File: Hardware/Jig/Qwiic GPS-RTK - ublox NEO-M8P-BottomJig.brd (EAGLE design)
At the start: 40.6 x 33 mm, 103 parts, among them J13 U.FL, J3 PTH, U1 NEO-M8P, U2 3.3V

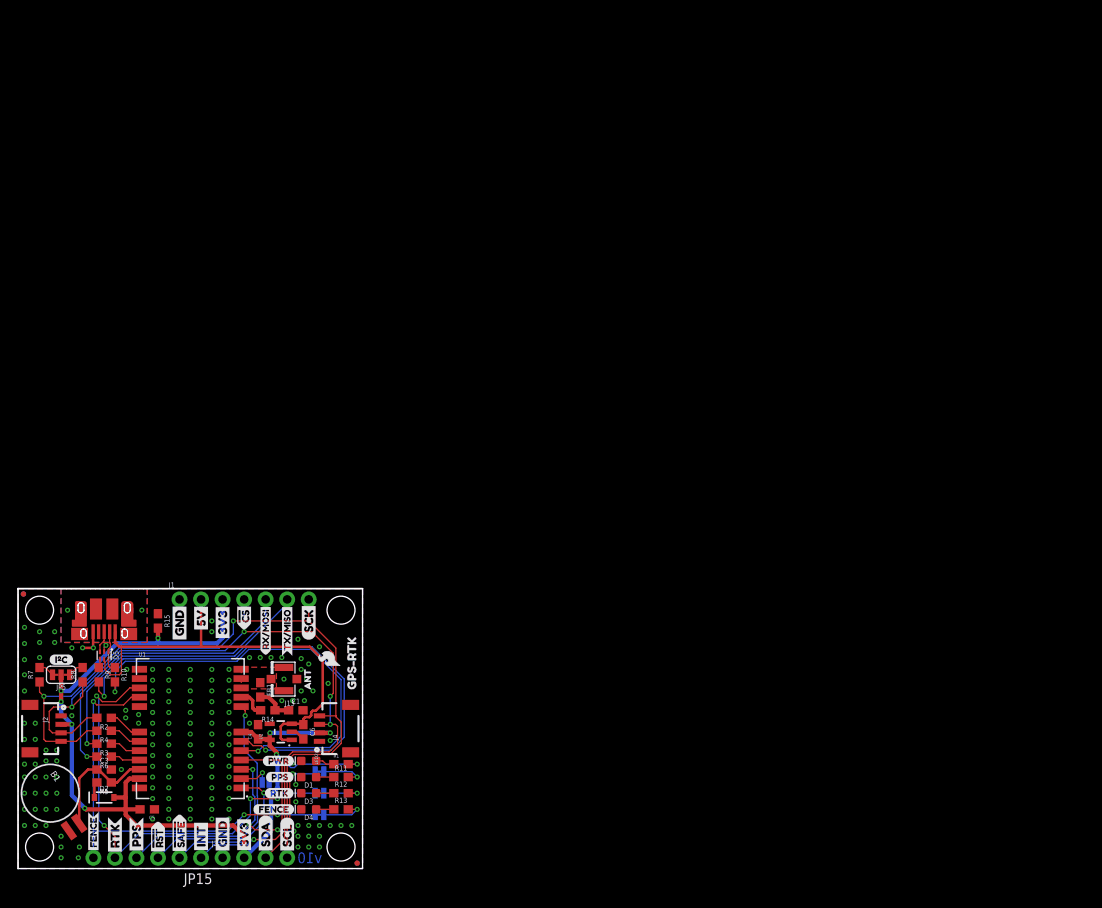
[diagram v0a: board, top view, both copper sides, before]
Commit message: Adding test jig
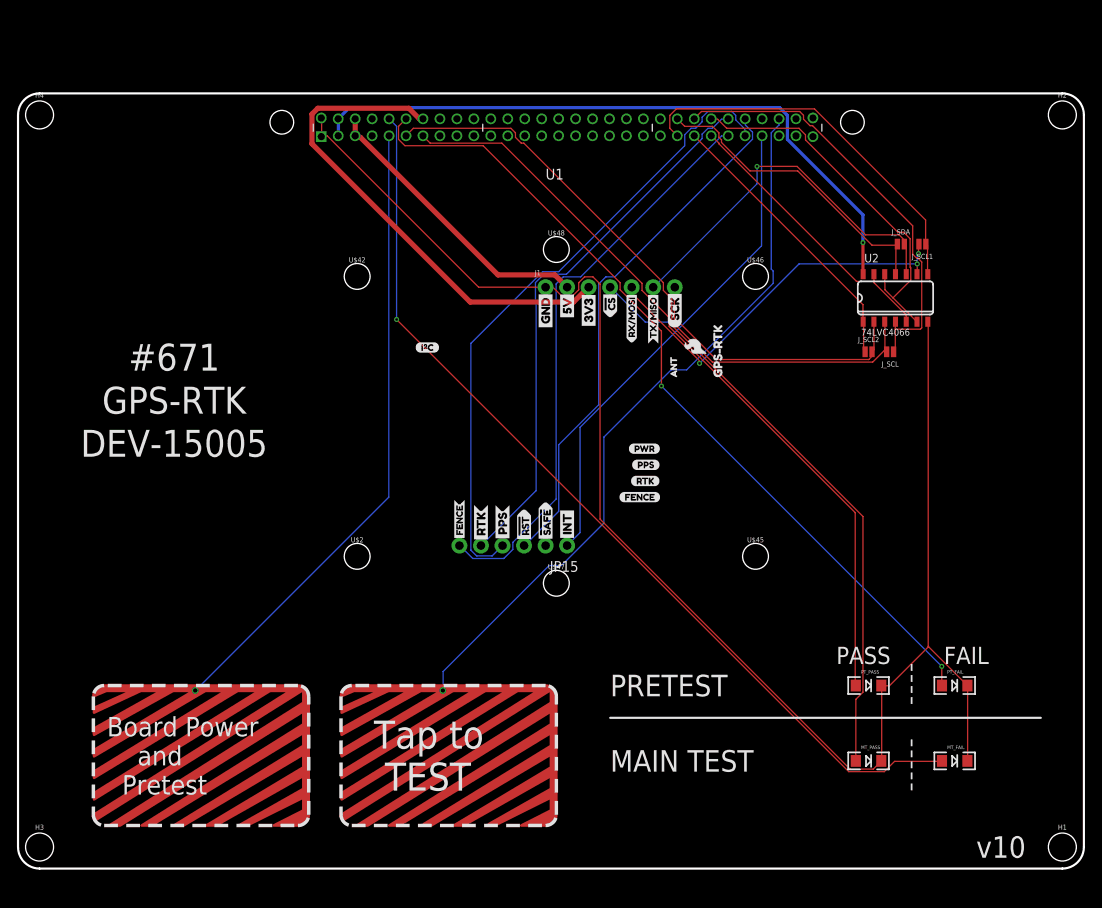
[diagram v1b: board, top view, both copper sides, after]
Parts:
- removed B1: 6.8MM_COIN_CELL, SparkFun-Batteries:BATTCON-6.8MM
- removed C1: 47pF, SparkFun-Capacitors:0603
- removed C3, C4, C6: 1.0uF, SparkFun-Capacitors:0603
- removed C5: 0.1uF, SparkFun-Capacitors:0603
- removed D1: Yellow, SparkFun-LED:LED-0603
- removed D2: 0.5A/40V/420mV, SparkFun-DiscreteSemi:SOD-323
- removed D3: GREEN, SparkFun-LED:LED-0603
- removed D4: BLUE, SparkFun-LED:LED-0603
- removed D5: PRTR5V0U2F, funbit:SOT886
- removed FB1: 30Ω/1.8A, SparkFun-Coils:0603
- removed FRAME1: FRAME-LETTER, SparkFun-Aesthetics:CREATIVE_COMMONS
- removed J13: U.FL, SparkFun-Connectors:U.FL
- removed J2, J4: (no value), SparkFun-Connectors:1X04_1MM_RA
- removed J3: PTH, SparkX:1X04_NO_SILK
- removed J6: (no value), SparkFun-Connectors:USB-MICROB-PTH-MILL
- removed JP1, JP2, JP3: (no value), SparkFun-Jumpers:SMT-JUMPER_2_NC_TRACE_SILK
- removed JP101, JP31, JP41, JP91: STAND-OFF, SparkFun:STAND-OFF
- removed JP21, JP61, JP71, JP81: FIDUCIALUFIDUCIAL, SparkFun:MICRO-FIDUCIAL
- removed JP4: (no value), SparkFun-Jumpers:SMT-JUMPER_2_NO_SILK
- removed JP5: (no value), SparkFun-Jumpers:SMT-JUMPER_3_2-NC_TRACE_SILK
- removed LED2: RED, SparkFun-LED:LED-0603
- removed LOGO1: OSHW-LOGOMINI, SparkFun-Aesthetics:OSHW-LOGO-MINI
- removed LOGO2: SFE_LOGO_NAME_FLAME.1_INCH, SparkFun-Aesthetics:SFE_LOGO_NAME_FLAME_.1
- removed R1, R11, R12, R13, R5: 1k, SparkFun-Resistors:0603
- removed R10, R9: 27, SparkFun-Resistors:0603
- removed R14: 10, SparkFun-Resistors:0603
- removed R15: 100k, SparkFun-Resistors:0603
- removed R2, R3, R4, R6: 33, SparkFun-Resistors:0603
- removed R7, R8: 2.2k, SparkFun-Resistors:0603
- removed U$1, U$4: (no value), Labels:SDA-[)
- removed U$3, U$5: (no value), Labels:SCL-[)
- removed U$6, U$7: (no value), Labels:3V3-04
- removed U$8, U$9: (no value), Labels:GND-04
- added BUTTON1, BUTTON2: CAPSENSE_BUTTON_PAD_ONLY, Testing:CAPSENSE_BUTTON_PADS_ONLY
- added FRAME2: FRAME-LEDGER, SparkFun-Aesthetics:CREATIVE_COMMONS
- added H1, H2, H3, H4: STAND-OFF, SparkFun-Hardware:STAND-OFF
- added J_SCL, J_SDA: JUMPER-SMT_2_NO_NO-SILK, SparkFun-Jumpers:SMT-JUMPER_2_NO_NO-SILK
- added J_SCL1, J_SCL2: (no value), SparkFun-Jumpers:SMT-JUMPER_2_NO_NO-SILK
- added MT_FAIL, MT_PASS, PT_FAIL, PT_PASS: (no value), Testing:LED-1206
- added U$2, U$42, U$45, U$46, U$47, U$48: (no value), SparkFun-Hardware:STAND-OFF-TIGHT
- U1: value NEO-M8P -> FLYING_JALAPENO; device NEO-M8P:NEO-M8P -> Testing:FLYING_JALAPENO_V3_M
- U2: value 3.3V -> 74LVC4066; device SparkFun-IC-Power:SOT23-5 -> Testing:SO14
- moved U2 88.2 mm to (102.9, 67.3), turned to 0 degrees
- moved U1 87.1 mm to (64.8, 91.4)
- moved U$13 56.8 mm to (72.3, 45.7)
- moved U$19 56.8 mm to (64.8, 64.5)
- moved U$20 56.8 mm to (64.8, 64.5)
- moved U$22 56.8 mm to (68.5, 55.0)
- moved U$30 56.8 mm to (47.4, 45.6)
- moved U$33 56.8 mm to (81.5, 60.5)
- moved U$34 56.8 mm to (74.9, 61.8)
- moved U$37 56.8 mm to (74.9, 61.0)
- moved U$53 56.8 mm to (71.1, 49.0)
- moved U$55 56.8 mm to (77.3, 57.3)
- moved U$60 56.8 mm to (67.3, 63.5)
- moved U$61 56.8 mm to (67.3, 63.5)
- moved J1 56.8 mm to (62.2, 68.6)
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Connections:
- removed net 3.3V: C4.1, C5.2, D2.A, J1.3, J2.2, J3.2, J4.2, JP5.2, R1.2, R15.2, U1.23, U1.7, U2.5
- removed net 5V: C6.1, D5.5, J1.2, J6.VBUS, U2.1, U2.3
- removed net ANT_VCC: C1.1, FB1.2, R14.1
- removed net BACKUP: B1.+, C3.1, R5.1, U1.22
- removed net D+: D5.4, R9.1
- removed net D-: D5.6, R10.1
- removed net D_SEL: JP4.2, U1.2
- removed net GPS_ANT1: FB1.1, J13.FEED, U1.11
- removed net N$1: D3.A, R12.1
- removed net N$10: LED2.A, R1.1
- removed net N$11: R9.2, U1.6
- removed net N$12: R10.2, U1.5
- removed net N$13: R14.2, U1.9
- removed net N$2: D1.A, R11.1
- removed net N$3: JP2.1, R12.2
- removed net N$4: JP1.1, R11.2
- removed net N$5: JP5.1, R8.2
- removed net N$6: D2.C, R5.2
- removed net N$7: D4.A, R13.1
- removed net N$8: JP5.3, R7.2
- removed net N$9: JP3.1, R13.2
- removed net RXLV: R6.1, U1.21
- removed net SCL_LV: R4.1, U1.19
- removed net SDA_LV: R2.1, U1.18
- removed net SHLD: J6.SHIELD, J6.SHIELD10, J6.SHIELD2, J6.SHIELD3, J6.SHIELD4, J6.SHIELD5, J6.SHIELD6, J6.SHIELD7, J6.SHIELD8, J6.SHIELD9
- removed net TXLV: R3.1, U1.20
- removed net USB_D+: D5.3, J6.D+
- removed net USB_D-: D5.1, J6.D-
- new net 3.3V_POWER: U1.2, U1.32, U2.14
- new net 3V3_OUT_FROM_GPS: J1.3, U1.37
- new net 5V_POWER: J1.2, U1.3, U1.33
- new net JALAPENO_CS: U1.60
- new net JALAPENO_I2C_EN: U1.24, U2.13, U2.5
- new net JALAPENO_MISO: U1.29
- new net JALAPENO_MOSI: U1.59
- new net JALAPENO_RX1-I: J_SDA.1, U1.52, U2.11
- new net JALAPENO_SCK: U1.30
- new net JALAPENO_SCL: J_SCL.1, U1.53, U2.4
- new net JALAPENO_SDA: J_SCL2.1, U1.23, U2.1
- new net JALAPENO_SERIAL_EN: U1.54, U2.12, U2.6
- new net JALAPENO_TX1-O: J_SCL1.1, U1.22, U2.8
- new net J_29: U1.57
- new net J_30: U1.28
- new net J_A1: U1.8
- new net J_A2: U1.38
- new net J_A3: U1.9
- new net J_A4: U1.39
- new net J_PWM2: U1.14
- new net J_PWM3: U1.44
- new net J_PWM4: U1.15
- new net J_PWM5: U1.45
- new net N$14: PT_PASS.A, U1.7
- new net N$15: PT_FAIL.A, U1.36
- new net N$16: MT_PASS.A, U1.6
- new net N$17: MT_FAIL.A, U1.35
- new net N$18: BUTTON2.CAPSENSE_PAD, U1.58
- new net N$19: BUTTON1.CAPSENSE_PAD, U1.5
- net !RESET: now also U1.56; no longer U1.8
- net !SAFE: no longer U1.1
- net FENCE_STAT: now also U1.25; no longer JP3.2, U1.16
- net GND: now also MT_FAIL.C, MT_PASS.C, PT_FAIL.C, PT_PASS.C, U1.1, U1.31, U2.7; no longer B1.-, C1.2, C3.2, C4.2, C5.1, C6.2, D1.C, D3.C, D4.C, D5.2, J13.1, J13.2, J2.1, J3.1, J4.1, J6.GND, JP4.1, LED2.C, R15.1, U1.10, U1.12, U1.13, U1.24, U2.2
- net INT: now also U1.27; no longer U1.4
- net PPS: now also U1.26; no longer JP1.2, U1.3
- net RTK_STAT: now also U1.55; no longer JP2.2, U1.15
- net RXI/MOSI: now also J_SCL1.2, U2.9; no longer R6.2
- net SCL/SCK: now also J_SCL.2, U2.3; no longer J2.4, J3.4, J4.4, R4.2, R7.1
- net SDA/!CS: now also J_SCL2.2, U2.2; no longer J2.3, J3.3, J4.3, R2.2, R8.1
- net TXO/MISO: now also J_SDA.2, U2.10; no longer R3.2
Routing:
- net GND: track 5.71 -> 188.6 mm, vias 161 -> 0
- net 3.3V: track 118.9 -> 0.00 mm, vias 9 -> 0
- net N$17: track 0.00 -> 111.0 mm, vias 0 -> 1
- net N$16: track 0.00 -> 105.1 mm
- net N$15: track 0.00 -> 99.2 mm, vias 0 -> 2
- net N$14: track 0.00 -> 91.0 mm
- net N$18: track 0.00 -> 86.0 mm
- net 3.3V_POWER: track 0.00 -> 78.4 mm, vias 0 -> 1
- net N$19: track 0.00 -> 74.9 mm
- net 3V3_OUT_FROM_GPS: track 0.00 -> 58.5 mm
- net N$11: track 55.6 -> 0.00 mm, vias 2 -> 0
- net 5V: track 53.6 -> 0.00 mm
- net SCL/SCK: track 88.9 -> 35.5 mm, vias 2 -> 0
- net N$12: track 52.2 -> 0.00 mm, vias 2 -> 0
- net JALAPENO_SCL: track 0.00 -> 51.4 mm
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- removed copper zone on layer 1, net GND
- removed copper zone on layer 16, net GND
- removed copper zone on layer 1, net GPS_ANT1
- removed copper zone on layer 1, net SHLD
- removed copper zone on layer 16, net SHLD
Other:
- board size 40.6 x 33 mm -> 125.7 x 91.4 mm
- board text added: "#671"
- board text added: "Board Power and Pretest"
- board text added: "DEV-15005"
- board text added: "FAIL"
- board text added: "GPS-RTK"
- board text added: "MAIN TEST"
- board text added: "PASS"
- board text added: "PRETEST"
- board text added: "Tap to TEST"

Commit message: Updating test jig to one button, add ground plane.
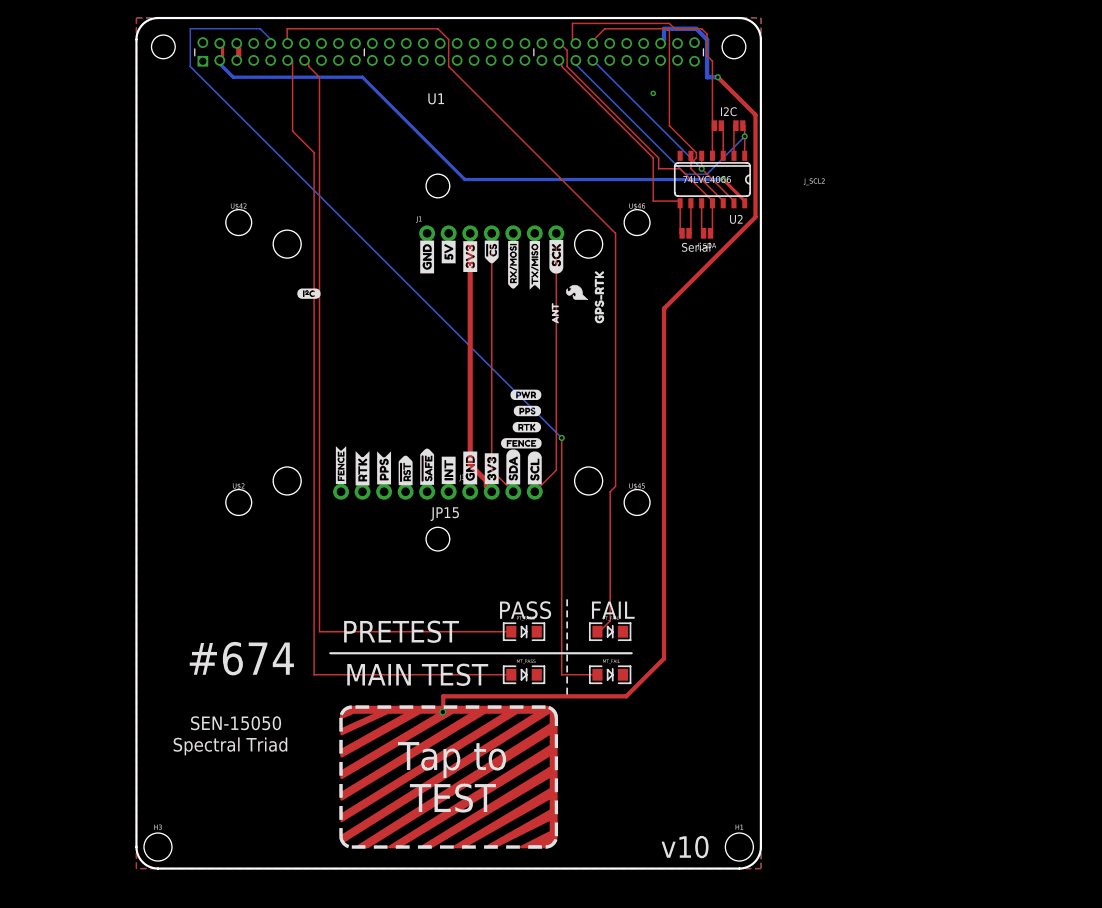
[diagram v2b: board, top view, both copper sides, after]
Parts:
- removed BUTTON1: CAPSENSE_BUTTON_PAD_ONLY, Testing:CAPSENSE_BUTTON_PADS_ONLY
- removed H2, H4: STAND-OFF, SparkFun-Hardware:STAND-OFF
- added FRAME1: FRAME-LETTER, SparkFun-Aesthetics:CREATIVE_COMMONS
- added J3: PTH, SparkX:1X04_NO_SILK
- added JP101, JP31, JP41, JP91: STAND-OFF, SparkFun:STAND-OFF
- added LOGO1: OSHW-LOGOMINI, SparkFun-Aesthetics:OSHW-LOGO-MINI
- added LOGO2: SFE_LOGO_NAME_FLAME.1_INCH, SparkFun-Aesthetics:SFE_LOGO_NAME_FLAME_.1
- added U$1, U$4: (no value), Labels:SDA-[)
- added U$3, U$5: (no value), Labels:SCL-[)
- added U$6, U$7: (no value), Labels:3V3-04
- added U$8, U$9: (no value), Labels:GND-04
- U$47, U$48: device SparkFun-Hardware:STAND-OFF-TIGHT -> SparkFun-Hardware:NUBBIN_LOCKER
- moved MT_FAIL 41.9 mm to (69.8, 22.9)
- moved MT_PASS 41.9 mm to (59.7, 22.9)
- moved PT_FAIL 41.1 mm to (69.8, 27.9)
- moved PT_PASS 41.1 mm to (59.7, 27.9)
- moved H1 38.1 mm to (85.1, 2.54)
- moved J_SCL 33.5 mm to (82.5, 87.6), turned to 0 degrees
- moved J_SCL2 30.7 mm to (85.1, 87.6), turned to 180 degrees
- moved J_SCL1 28.0 mm to (78.7, 74.9), turned to 0 degrees
- moved U2 24.7 mm to (82.5, 81.3), turned to 180 degrees
- moved J_SDA 22.9 mm to (81.3, 74.9), turned to 180 degrees
- moved U1 16.6 mm to (50.8, 100.3)
- moved U$48 15.9 mm to (49.5, 80.5)
- moved U$33 15.3 mm to (67.6, 66.8)
- moved J1 15.3 mm to (48.3, 74.9)
- moved U$13 15.3 mm to (58.3, 52.1)
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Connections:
- net N$18 renamed BUTTON2
- removed net 3V3_OUT_FROM_GPS: J1.3, U1.37
- removed net N$19: BUTTON1.CAPSENSE_PAD, U1.5
- new net 3.3V: J1.3, J3.2
- new net 5V: J1.2
- new net JALAPENO_SPI_EN: U1.25
- new net J_25: U1.55
- new net J_26: U1.26
- new net J_27: U1.56
- new net J_28: U1.27
- new net J_A0: U1.37
- new net TARGET_RX: J_SCL1.2, U2.9
- new net TARGET_SCL: J_SCL.2, U2.3
- new net TARGET_SDA: J_SCL2.2, U2.2
- new net TARGET_TX: J_SDA.2, U2.10
- net !RESET: no longer U1.56
- net 5V_POWER: no longer J1.2
- net FENCE_STAT: no longer U1.25
- net GND: now also J3.1
- net INT: no longer U1.27
- net PPS: no longer U1.26
- net RTK_STAT: no longer U1.55
- net RXI/MOSI: no longer J_SCL1.2, U2.9
- net SCL/SCK: now also J3.4; no longer J_SCL.2, U2.3
- net SDA/!CS: now also J3.3; no longer J_SCL2.2, U2.2
- net TXO/MISO: no longer J_SDA.2, U2.10
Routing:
- net GND: track 188.6 -> 0.00 mm, vias 0 -> 1
- net PPS: track 75.6 -> 0.00 mm
- net N$19: track 74.9 -> 0.00 mm
- net FENCE_STAT: track 68.3 -> 0.00 mm
- net RTK_STAT: track 64.8 -> 0.00 mm
- net !RESET: track 62.5 -> 0.00 mm
- net 3V3_OUT_FROM_GPS: track 58.5 -> 0.00 mm
- net INT: track 57.9 -> 0.00 mm
- net RXI/MOSI: track 46.5 -> 0.00 mm, vias 3 -> 0
- net TXO/MISO: track 44.4 -> 0.00 mm, vias 1 -> 0
- net 5V_POWER: track 34.4 -> 2.17 mm
- net BUTTON2: track 86.0 -> 117.9 mm, vias 0 -> 1
- net 3.3V: track 0.00 -> 31.5 mm
- net JALAPENO_SCL: track 51.4 -> 33.7 mm
- net JALAPENO_TX1-O: track 45.2 -> 28.5 mm
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- added copper zone on layer 1, net GND
- added copper zone on layer 16, net GND
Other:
- board size 125.7 x 91.4 mm -> 73.7 x 100.3 mm
- board text added: "#674"
- board text added: "I2C"
- board text added: "SEN-15050"
- board text added: "Serial"
- board text added: "Spectral Triad"
- board text removed: "#671"
- board text removed: "Board Power and Pretest"
- board text removed: "DEV-15005"
- board text removed: "GPS-RTK"
